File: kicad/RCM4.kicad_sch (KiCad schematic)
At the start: 7 parts

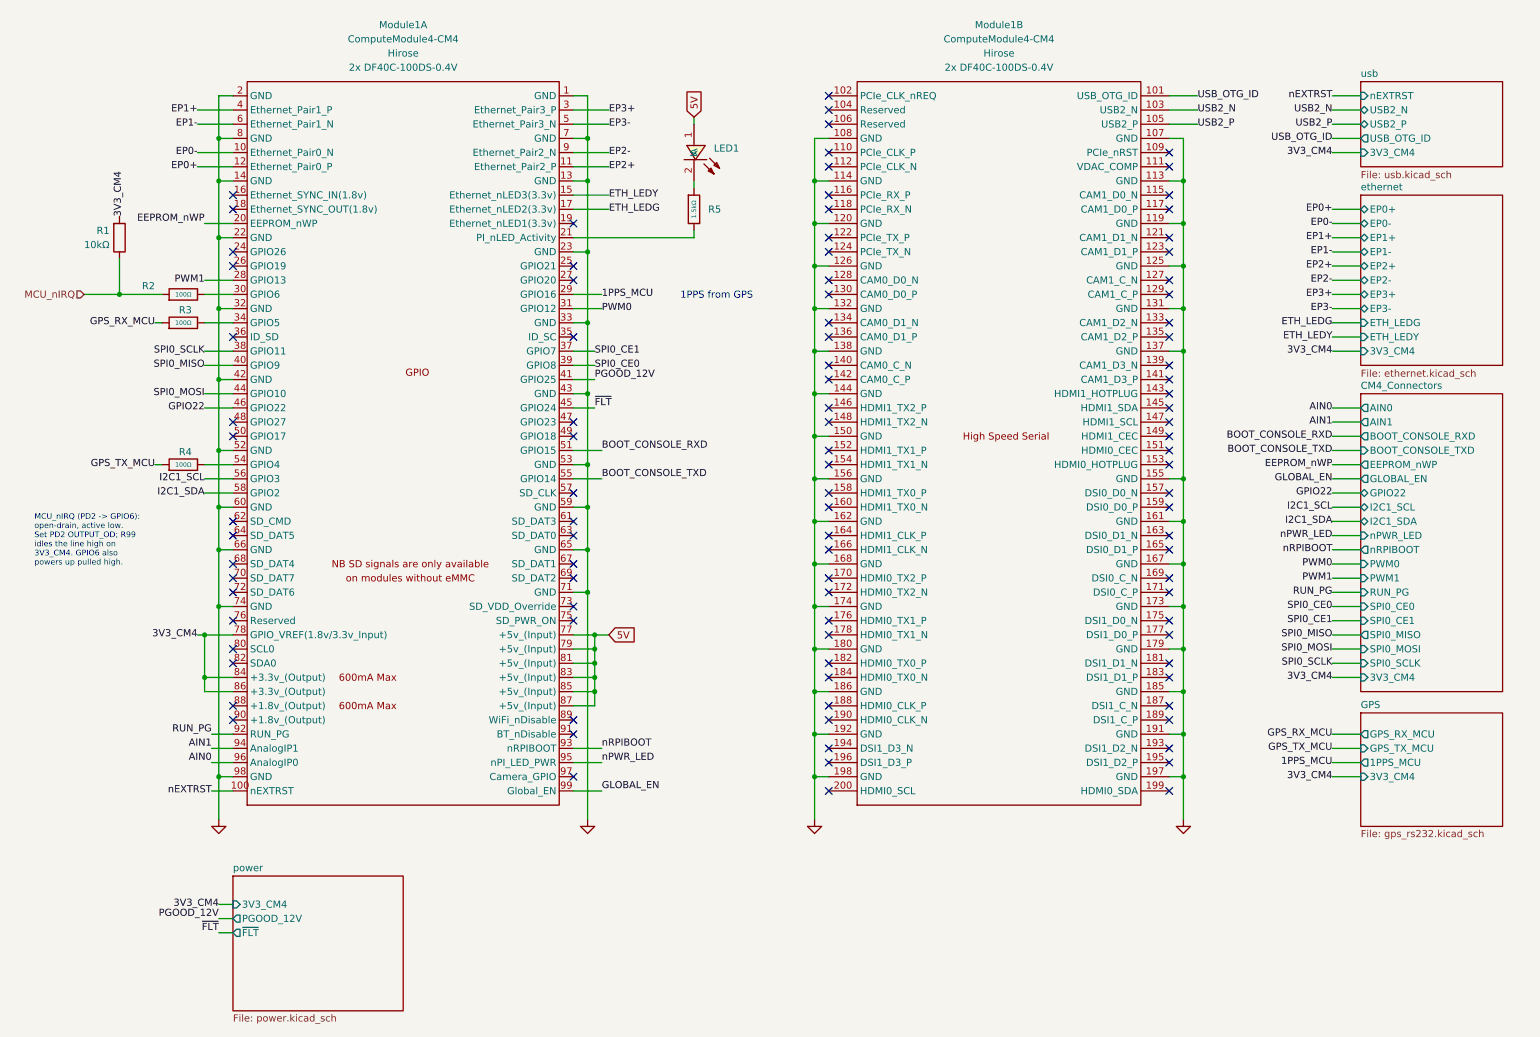
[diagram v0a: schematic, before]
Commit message: GPIO connectors defined
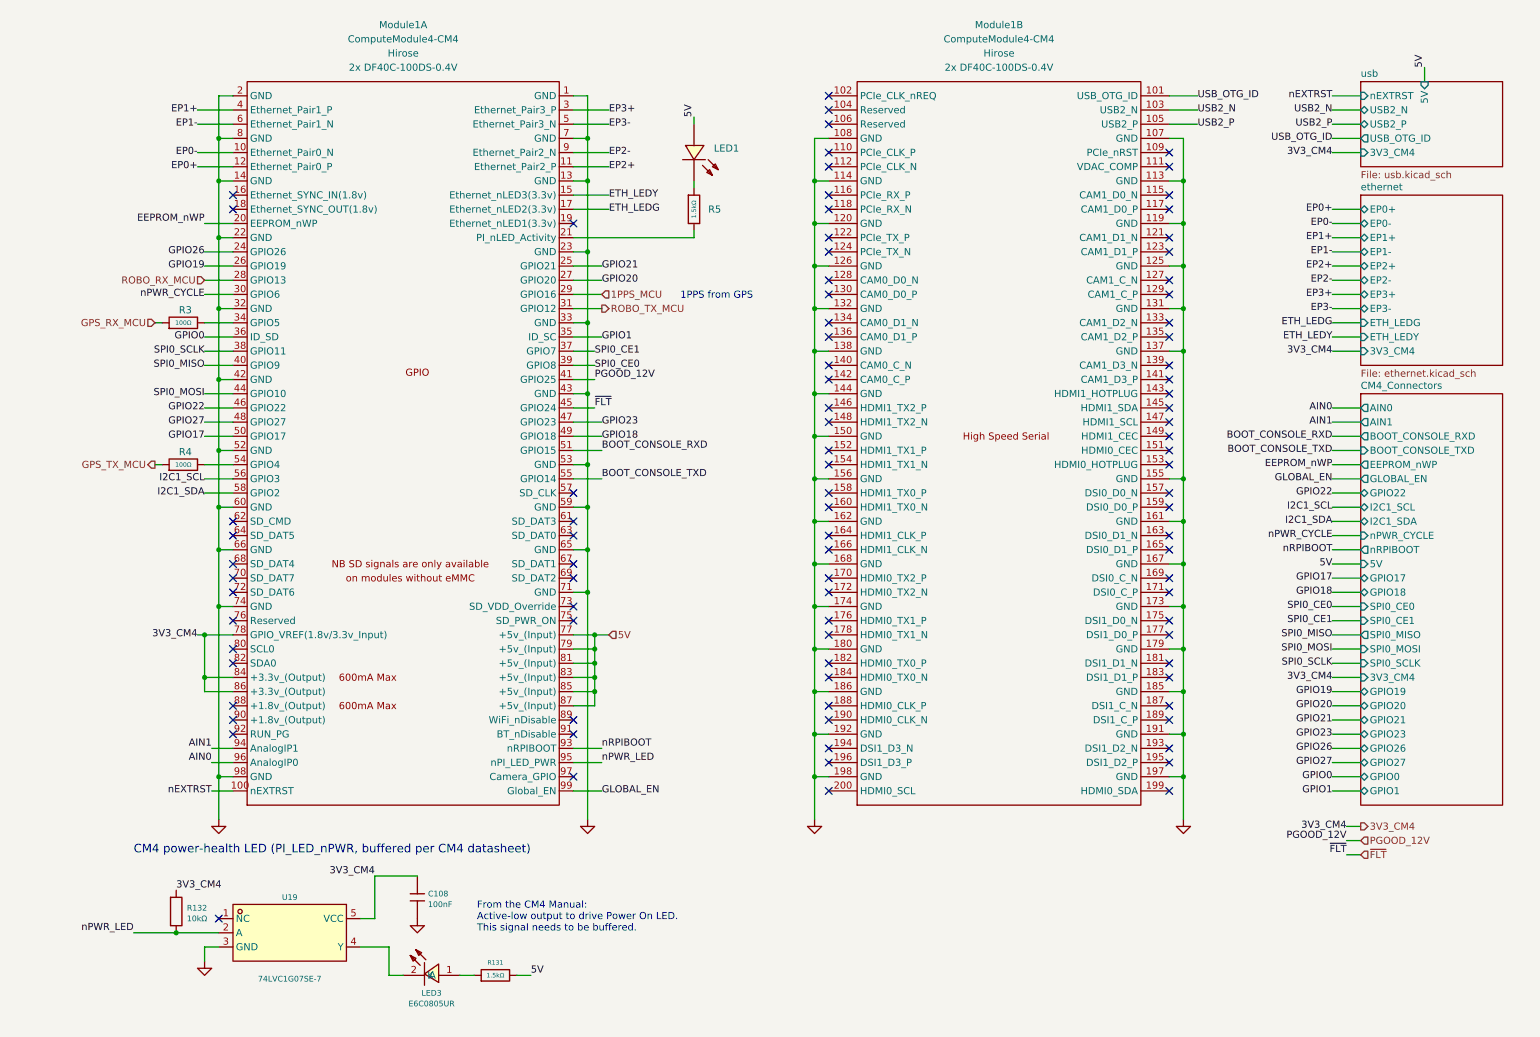
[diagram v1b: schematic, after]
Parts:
- removed R1: 10kΩ, PCM_JLCPCB:R_0402, symbol PCM_JLCPCB-Resistors:0402,10kΩ
- removed R2: 100Ω, PCM_JLCPCB:R_0402, symbol PCM_JLCPCB-Resistors:0402,100Ω
- added C108: 100nF, MyParts:C0402, symbol MyParts:CL05B104KO5NNNC_ALT
- added LED3: E6C0805UR, MyParts:LED0805-R-RD, symbol MyParts:E6C0805UR
- added R131: 1.5kΩ, MyParts:R0402, symbol MyParts:0402WGF1501TCE
- added R132: 10kΩ, MyParts:R0402, symbol MyParts:0402WGF1002TCE
- added U19: 74LVC1G07SE-7, MyParts:SC-88A_L2.0-W1.3-P0.65-LS2.1-BL, symbol MyParts:74LVC1G07SE-7
- LED1: value RED -> GREEN; symbol MyParts:E6C0805UR -> MyParts:0805G; LCSC Part C2295 -> C2297; MPN KT-0805R -> KT-0805G
- Module1: footprint CM4_PARTS:Raspberry-Pi-4-Compute-Module -> MyParts:Raspberry-Pi-4-Compute-Module; symbol CM4Parts:ComputeModule4-CM4 -> MyParts:ComputeModule4-CM4
- R3, R4: footprint PCM_JLCPCB:R_0402 -> MyParts:R0402; symbol PCM_JLCPCB-Resistors:0402,100Ω -> MyParts:0402WGF1000TCE; Attrition Qty 10 -> (none); Category Resistors,Chip Resistor - Surface Mount -> (none); Class Basic Component -> (none); LCSC C25076 -> (none); LCSC Part (none) -> C25076; MPN (none) -> 0402WGF1000TCE; Manufacturer UNI-ROYAL(Uniroyal Elec) -> UNI-ROYAL; Minimum Qty 20 -> (none); Operating Temperature Range -55°C~+155°C -> (none); Overload Voltage (Max) 50V -> (none); Part 0402WGF1000TCE -> (none); Power(Watts) 62.5mW -> (none); Price 0.004USD -> (none); Process SMT -> (none); Resistance 100Ω -> (none); Stock 5907585 -> (none); Temperature Coefficient ±200ppm/°C -> (none); Type Thick Film Resistors -> (none); Voltage Rating (none) -> 50V
- R5: footprint PCM_JLCPCB:R_0402 -> MyParts:R0402; symbol PCM_JLCPCB-Resistors:0402,1.5kΩ -> MyParts:0402WGF1501TCE; Attrition Qty 10 -> (none); Category Resistors,Chip Resistor - Surface Mount -> (none); Class Basic Component -> (none); LCSC C25867 -> (none); LCSC Part (none) -> C25867; MPN (none) -> 0402WGF1501TCE; Manufacturer UNI-ROYAL(Uniroyal Elec) -> UNI-ROYAL; Minimum Qty 20 -> (none); Operating Temperature Range -55°C~+155°C -> (none); Overload Voltage (Max) 50V -> (none); Part 0402WGF1501TCE -> (none); Power(Watts) 62.5mW -> (none); Price 0.004USD -> (none); Process SMT -> (none); Resistance 1.5kΩ -> (none); Stock 1178558 -> (none); Temperature Coefficient ±100ppm/°C -> (none); Type Thick Film Resistors -> (none); Voltage Rating (none) -> 50V
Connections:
- net 3V3_CM4: now also C108.1, R132.1, U19.5 (VCC)
- net 5V: now also R131.2
- net GND: now also C108.2, U19.3 (GND)
- net nPWR_LED: now also R132.2, U19.2 (A)
- net nPWR_CYCLE: now reaches Module1.30 (GPIO6)
- net GPIO26: now reaches Module1.24 (GPIO26)
- net GPIO21: now reaches Module1.25 (GPIO21)
- net GPIO19: now reaches Module1.26 (GPIO19)
- net GPIO20: now reaches Module1.27 (GPIO20)
- net GPIO1: now reaches Module1.35 (ID_SC)
- net GPIO0: now reaches Module1.36 (ID_SD)
- net GPIO23: now reaches Module1.47 (GPIO23)
- net GPIO27: now reaches Module1.48 (GPIO27)
- net GPIO18: now reaches Module1.49 (GPIO18)
- net GPIO17: now reaches Module1.50 (GPIO17)
- net PWM0 renamed ROBO_TX_MCU
- net PWM1 renamed ROBO_RX_MCU
- net RUN_PG: no longer names the net of Module1.92 (RUN_PG)
- new net: LED3.1 (A), R131.1
- new net: LED3.2 (K), U19.4 (Y)
- no-connect marks 100 -> 92
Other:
- removed sheet GPS
- removed sheet power
- sheet CM4_Connectors ports: added 5V, GPIO0, GPIO1, GPIO17, GPIO18, GPIO19, GPIO20, GPIO21, GPIO23, GPIO26, GPIO27, nPWR_CYCLE; removed PWM0, PWM1, RUN_PG, nPWR_LED
- sheet usb ports: added 5V; removed none
- note added: "CM4 power-health LED (PI_LED_nPWR, buffered per CM4 datasheet)"
- note added: "From the CM4 Manual: Active-low output to drive Power On LED. This signal needs to be buffered."
- note removed: "MCU_nIRQ (PD2 -> GPIO6): open-drain, active low. Set PD2 OUTPUT_OD; R99 idles the line high on 3V3_CM4. GPIO6 also powers up pulled high."

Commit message: schematic cleanup
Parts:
- added R133, R134: 1kΩ, MyParts:R0402, symbol MyParts:0402WGF1001TCE
- added TP12, TP13, TP14, TP22: TestPoint_Small, TestPoint:TestPoint_Pad_D1.5mm, symbol Connector:TestPoint_Small
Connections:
- net AIN0: now also R133.1; no longer Module1.96 (AnalogIP0)
- net AIN1: now also R134.1; no longer Module1.94 (AnalogIP1)
- net GND: now also TP12.1, TP22.1
- net at LED1.2 (K), R5.1: now also TP13.1
- net at LED3.2 (K), U19.4 (Y): now also TP14.1
- new net: Module1.96 (AnalogIP0), R133.2
- new net: Module1.94 (AnalogIP1), R134.2

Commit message: Still refining
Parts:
- C108, R131, R132, R133, R134, R3, R4, R5: Pkg Type (none) -> SMD 0402
- LED1, LED3: Pkg Type (none) -> SMD 0805
- Module1: Pkg Type (none) -> SMD CM4 module (2x100-pin Hirose DF40)
- TP12, TP13, TP14, TP22: Pkg Type (none) -> SMD Test pad D1.5
- U19: Pkg Type (none) -> SMD SOT-353 (SC-88A)
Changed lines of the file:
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@@
 			)
 		)
+		(property "Pkg Type" "SMD 0402"
+			(at 43.18 147.32 0)
+			(hide yes)
+			(show_name no)
+			(do_not_autoplace no)
+			(effects
+				(font
+					(size 1.27 1.27)
+				)
+			)
+		)
 		(pin "1"
 		)
@@
 			)
 		)
+		(property "Pkg Type" "SMD 0805"
+			(at 134.62 38.1 0)
+			(hide yes)
+			(show_name no)
+			(do_not_autoplace no)
+			(effects
+				(font
+					(size 1.27 1.27)
+				)
+			)
+		)
 		(pin "1"
 		)
@@
 			)
 		)
+		(property "Pkg Type" "SMD 0402"
+			(at 97.79 185.42 0)
+			(hide yes)
+			(show_name no)
+			(do_not_autoplace no)
+			(effects
+				(font
+					(size 1.27 1.27)
+				)
+			)
+		)
 		(pin "1"
 		)
@@
 			)
 		)
+		(property "Pkg Type" "SMD 0805"
+			(at 86.36 184.15 0)
+			(hide yes)
+			(show_name no)
+			(do_not_autoplace no)
+			(effects
+				(font
+					(size 1.27 1.27)
+				)
+			)
+		)
 		(pin "1"
 		)
@@
 			)
 		)
+		(property "Pkg Type" "SMD 0402"
+			(at 133.35 48.26 0)
+			(hide yes)
+			(show_name no)
+			(do_not_autoplace no)
+			(effects
+				(font
+					(size 1.27 1.27)
+				)
+			)
+		)
 		(pin "2"
 		)
@@
 			)
 		)
+		(property "Pkg Type" "SMD CM4 module (2x100-pin Hirose DF40)"
+			(at 83.82 83.82 0)
+			(hide yes)
+			(show_name no)
+			(do_not_autoplace no)
+			(effects
+				(font
+					(size 1.27 1.27)
+				)
+			)
+		)
 		(pin "95"
 		)
@@
 			)
 		)
+		(property "Pkg Type" "SMD 0402"
+			(at 43.18 144.78 0)
+			(hide yes)
+			(show_name no)
+			(do_not_autoplace no)
+			(effects
+				(font
+					(size 1.27 1.27)
+				)
+			)
+		)
 		(pin "1"
 		)
@@
 			)
 		)
+		(property "Pkg Type" "SMD 0402"
+			(at 40.64 173.99 0)
+			(hide yes)
+			(show_name no)
+			(do_not_autoplace no)
+			(effects
+				(font
+					(size 1.27 1.27)
+				)
+			)
+		)
 		(pin "1"
 		)
@@
 			)
 		)
+		(property "Pkg Type" "SMD CM4 module (2x100-pin Hirose DF40)"
+			(at 48.26 88.9 0)
+			(hide yes)
+			(show_name no)
+			(do_not_autoplace no)
+			(effects
+				(font
+					(size 1.27 1.27)
+				)
+			)
+		)
 		(pin "95"
 		)
@@
 			)
 		)
+		(property "Pkg Type" "SMD Test pad D1.5"
+			(at 153.67 142.24 0)
+			(hide yes)
+			(show_name no)
+			(do_not_autoplace no)
+			(effects
+				(font
+					(size 1.27 1.27)
+				)
+			)
+		)
 		(pin "1"
 		)
@@
 			)
 		)
+		(property "Pkg Type" "SMD Test pad D1.5"
+			(at 74.93 181.61 0)
+			(hide yes)
+			(show_name no)
+			(do_not_autoplace no)
+			(effects
+				(font
+					(size 1.27 1.27)
+				)
+			)
+		)
 		(pin "1"
 		)
@@
 			)
 		)
+		(property "Pkg Type" "SMD Test pad D1.5"
+			(at 153.67 149.86 0)
+			(hide yes)
+			(show_name no)
+			(do_not_autoplace no)
+			(effects
+				(font
+					(size 1.27 1.27)
+				)
+			)
+		)
 		(pin "1"
 		)
@@
 			)
 		)
+		(property "Pkg Type" "SMD SOT-353 (SC-88A)"
+			(at 60.96 177.8 0)
+			(hide yes)
+			(show_name no)
+			(do_not_autoplace no)
+			(effects
+				(font
+					(size 1.27 1.27)
+				)
+			)
+		)
 		(pin "1"
 		)
@@
 			)
 		)
+		(property "Pkg Type" "SMD Test pad D1.5"
+			(at 132.08 43.18 0)
+			(hide yes)
+			(show_name no)
+			(do_not_autoplace no)
+			(effects
+				(font
+					(size 1.27 1.27)
+				)
+			)
+		)
 		(pin "1"
 		)
@@
 			)
 		)
+		(property "Pkg Type" "SMD 0402"
+			(at 41.91 68.58 0)
+			(hide yes)
+			(show_name no)
+			(do_not_autoplace no)
+			(effects
+				(font
+					(size 1.27 1.27)
+				)
+			)
+		)
 		(pin "1"
 		)
@@
 			)
 		)
+		(property "Pkg Type" "SMD 0402"
+			(at 41.91 93.98 0)
+			(hide yes)
+			(show_name no)
+			(do_not_autoplace no)
+			(effects
+				(font
+					(size 1.27 1.27)
+				)
+			)
+		)
 		(pin "1"
 		)
@@
 			(at 83.82 171.45 0)
 			(hide yes)
+			(show_name no)
+			(do_not_autoplace no)
+			(effects
+				(font
+					(size 1.27 1.27)
+				)
+			)
+		)
+		(property "Pkg Type" "SMD 0402"
+			(at 83.82 171.45 0)
+			(hide yes)

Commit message: Mods
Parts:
- added D54, D55: BAT54S, MyParts:SOT-23-3_L2.9-W1.6-P1.90-LS2.8-BR, symbol MyParts:BAT54S
- added TP30: TestPoint_Small, TestPoint:TestPoint_Pad_D1.5mm, symbol Connector:TestPoint_Small
- R133, R134: value 1kΩ -> 10kΩ; symbol MyParts:0402WGF1001TCE -> MyParts:0402WGF1002TCE; LCSC Part C11702 -> C25744; MPN 0402WGF1001TCE -> 0402WGF1002TCE
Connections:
- net 3V3_CM4: now also D54.2 (K), D55.2 (K)
- net ETH_LEDG: now also Module1.15 (Ethernet_nLED3(3.3v)); no longer Module1.17 (Ethernet_nLED2(3.3v))
- net ETH_LEDY: now also Module1.17 (Ethernet_nLED2(3.3v)); no longer Module1.15 (Ethernet_nLED3(3.3v))
- net GND: now also D54.1 (A), D55.1 (A), TP30.1
- net AIP0: now reaches Module1.96 (AnalogIP0), R133.2
- net AIP0: now also D55.3 (AK)
- net AIP1: now reaches Module1.94 (AnalogIP1), R134.2
- net AIP1: now also D54.3 (AK)
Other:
- note added: "Module1 pins 89 (WiFi_nDisable) and 91 (BT_nDisable) are left unconnected on purpose. This board needs a CM4 WITHOUT wireless, where both pins are reserved (CM4 datasheet 2.1.1 / 2.1.2). If a wireless CM4 is ever fitted, disable the radios in config.txt: dtoverlay=disable-wifi and dtoverlay=disable-bt (the latter also frees UART0)."
- moved on the sheet: C108, LED3, R131, R132, R133, R134, TP14, U19
